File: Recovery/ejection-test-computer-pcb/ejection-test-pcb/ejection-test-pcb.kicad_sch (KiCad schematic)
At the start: 22 parts, among them J1 BATTERY_TERMINAL, J2 LOAD_CELL_CONNECTOR, J3 NICHROME-TERMINAL, Q1 IRLZ34N, SW1 ON, U1 HX7111, U2 LM2596, U3 ESP32_DEVKIT

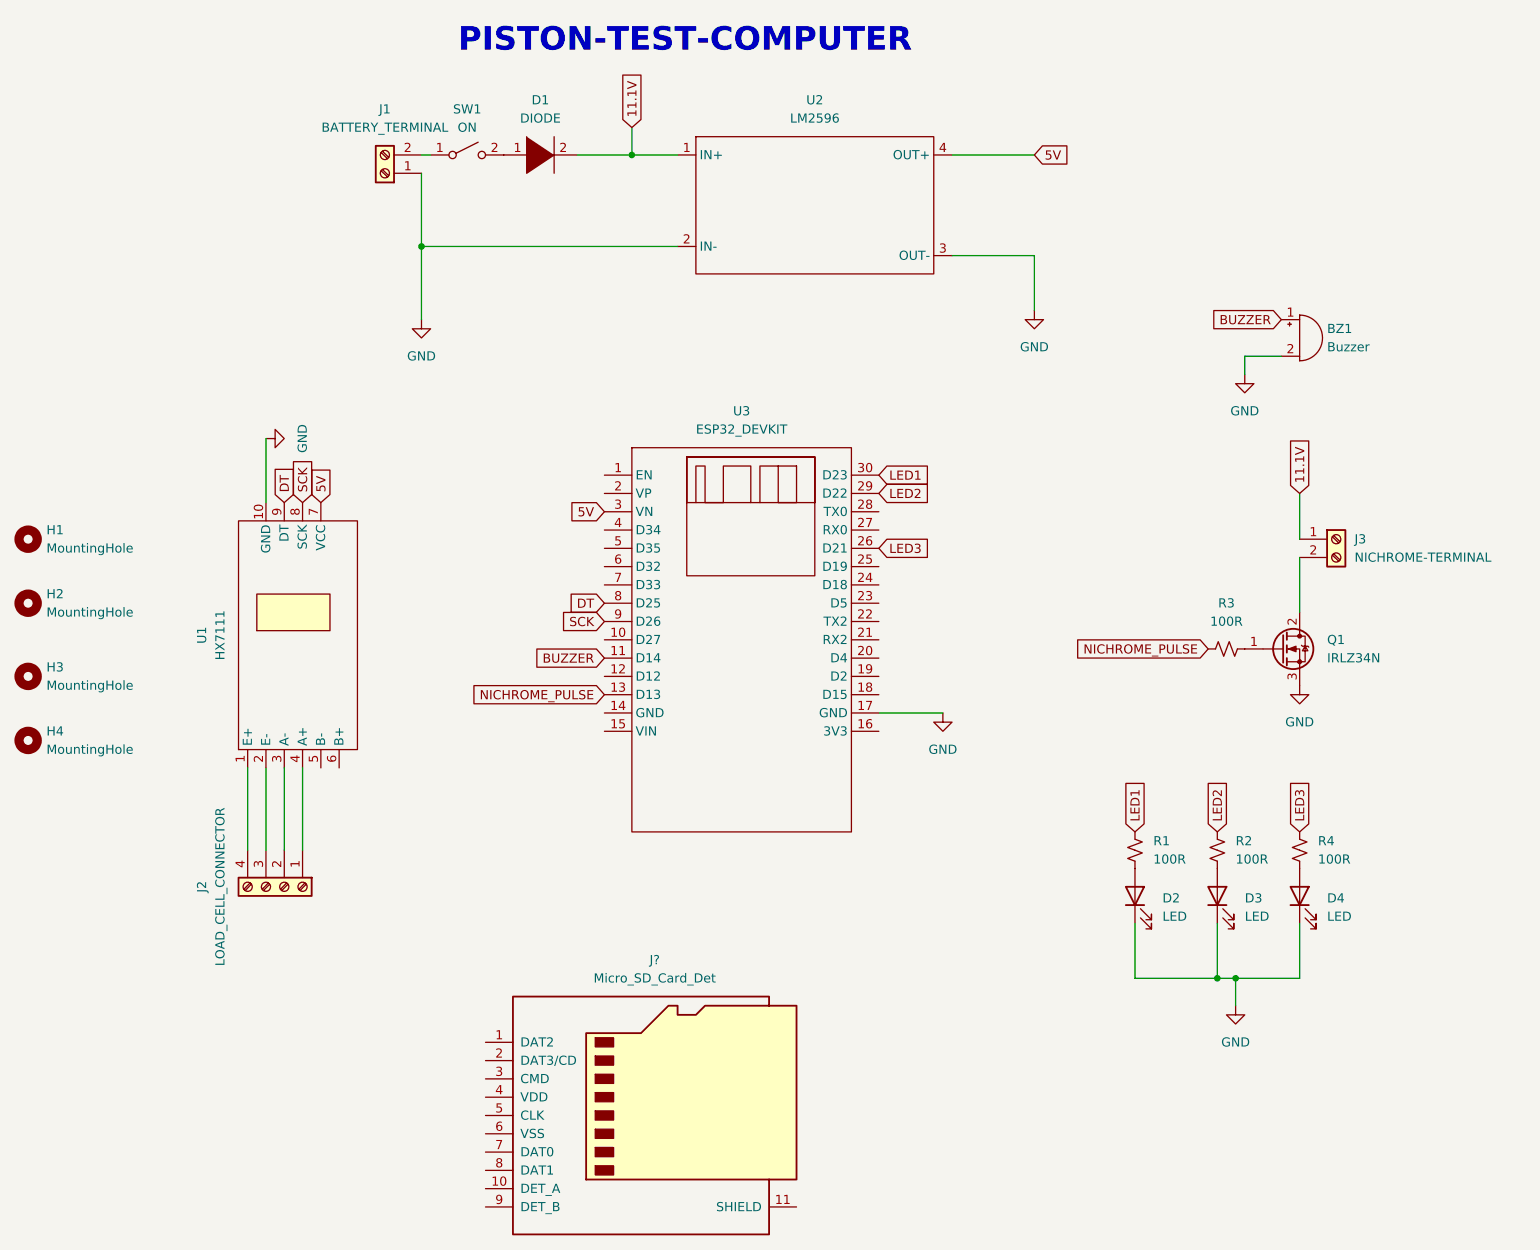
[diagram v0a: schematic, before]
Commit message: updated nichrome counter time
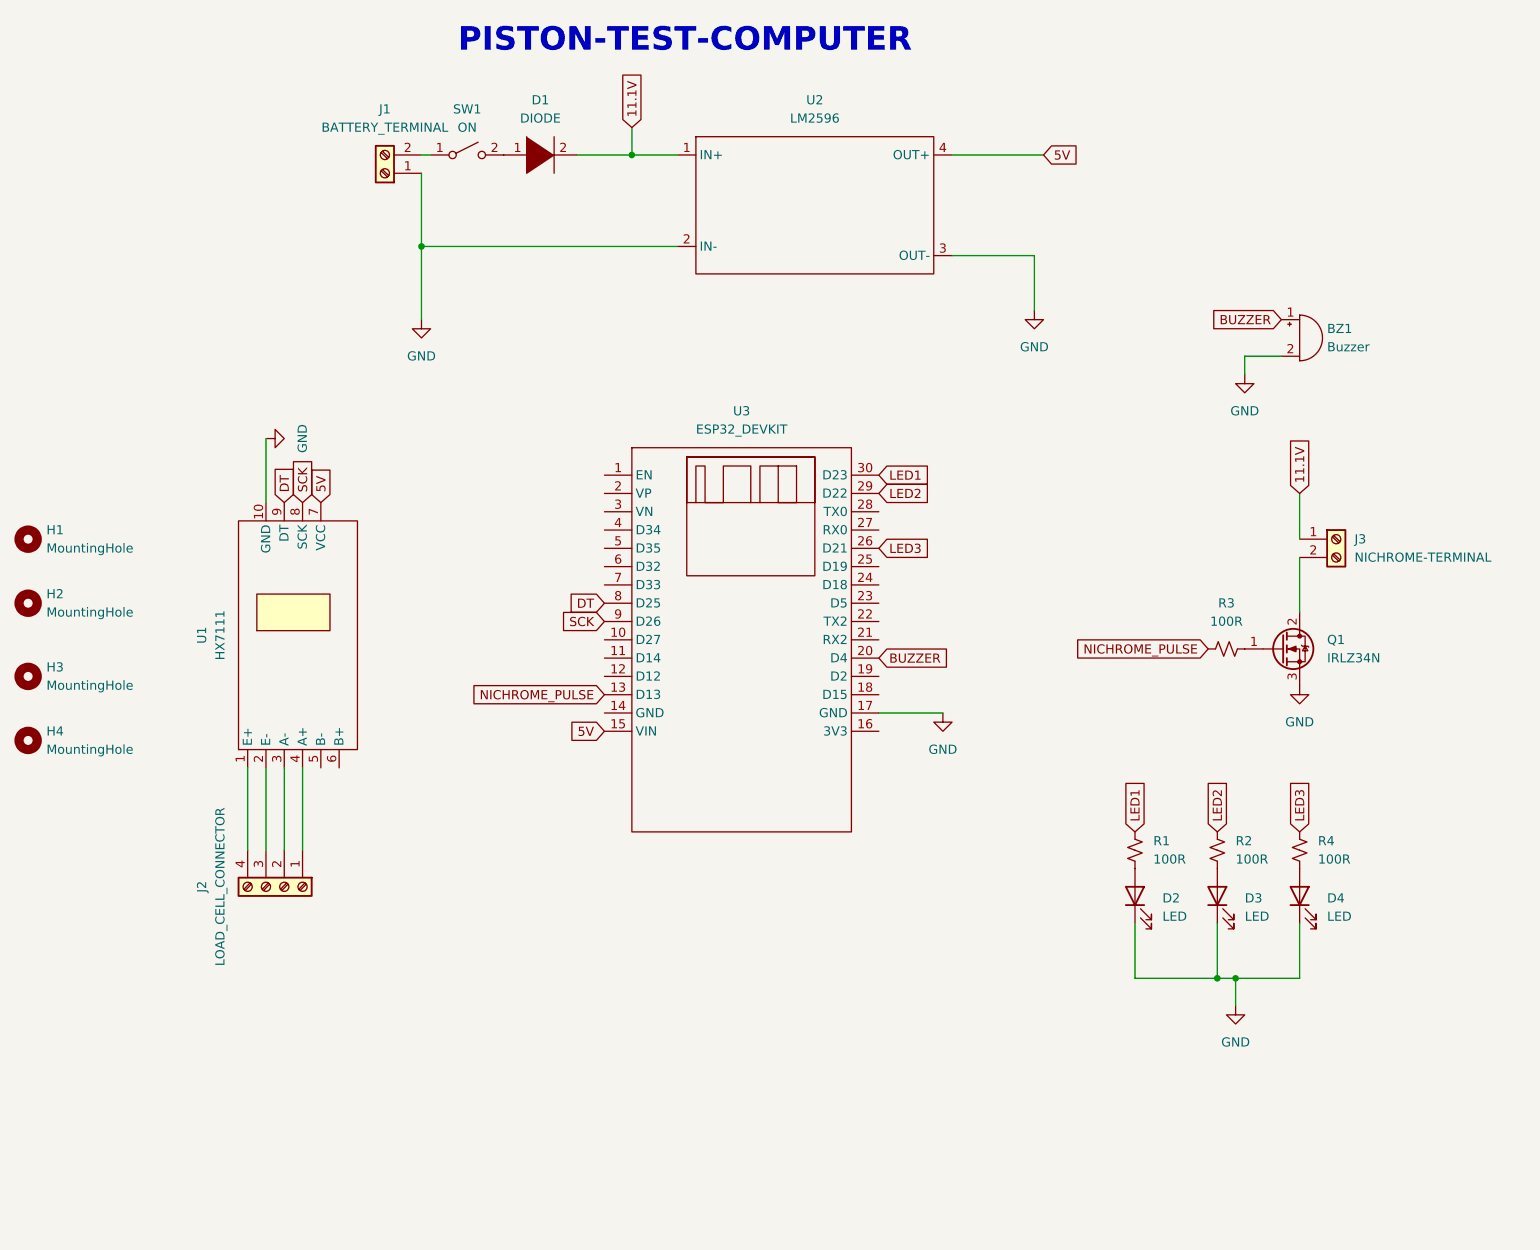
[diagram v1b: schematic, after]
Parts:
- removed J?: Micro_SD_Card_Det, symbol Connector:Micro_SD_Card_Det
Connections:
- net 5V: now also U3.15 (VIN); no longer U3.3 (VN)
- net BUZZER: now also U3.20 (D4); no longer U3.11 (D14)
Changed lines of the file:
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@@
     (stroke (width 0) (type default) (color 0 0 0 0))
   )
-  (wire (pts (xy 184.15 40.64) (xy 195.58 40.64))
+  (wire (pts (xy 184.15 40.64) (xy 196.85 40.64))
     (stroke (width 0) (type default) (color 0 0 0 0))
   )
@@
     )
   )
-  (global_label "5V" (shape input) (at 135.89 90.17 180) (fields_autoplaced)
+  (global_label "LED3" (shape input) (at 173.99 95.25 0) (fields_autoplaced)
+    (effects (font (size 1.27 1.27)) (justify left))
+    (property "Intersheet References" "${INTERSHEET_REFS}" (id 0) (at 181.0598 95.1706 0)
+      (effects (font (size 1.27 1.27)) (justify left) hide)
+    )
+  )
+  (global_label "5V" (shape input) (at 196.85 40.64 0) (fields_autoplaced)
+    (effects (font (size 1.27 1.27)) (justify left))
+    (property "Intersheet References" "${INTERSHEET_REFS}" (id 0) (at 201.5612 40.5606 0)
+      (effects (font (size 1.27 1.27)) (justify left) hide)
+    )
+  )
+  (global_label "LED1" (shape input) (at 209.55 134.62 90) (fields_autoplaced)
+    (effects (font (size 1.27 1.27)) (justify left))
+    (property "Intersheet References" "${INTERSHEET_REFS}" (id 0) (at 209.4706 127.5502 90)
+      (effects (font (size 1.27 1.27)) (justify left) hide)
+    )
+  )
+  (global_label "LED2" (shape input) (at 220.98 134.62 90) (fields_autoplaced)
+    (effects (font (size 1.27 1.27)) (justify left))
+    (property "Intersheet References" "${INTERSHEET_REFS}" (id 0) (at 220.9006 127.5502 90)
+      (effects (font (size 1.27 1.27)) (justify left) hide)
+    )
+  )
+  (global_label "11.1V" (shape input) (at 232.41 87.63 90) (fields_autoplaced)
+    (effects (font (size 1.27 1.27)) (justify left))
+    (property "Intersheet References" "${INTERSHEET_REFS}" (id 0) (at 232.3306 79.895 90)
+      (effects (font (size 1.27 1.27)) (justify left) hide)
+    )
+  )
+  (global_label "11.1V" (shape input) (at 139.7 36.83 90) (fields_autoplaced)
+    (effects (font (size 1.27 1.27)) (justify left))
+    (property "Intersheet References" "${INTERSHEET_REFS}" (id 0) (at 139.6206 29.095 90)
+      (effects (font (size 1.27 1.27)) (justify left) hide)
+    )
+  )
+  (global_label "5V" (shape input) (at 135.89 120.65 180) (fields_autoplaced)
     (effects (font (size 1.27 1.27)) (justify right))
-    (property "Intersheet References" "${INTERSHEET_REFS}" (id 0) (at 131.1788 90.0906 0)
+    (property "Intersheet References" "${INTERSHEET_REFS}" (id 0) (at 131.1788 120.7294 0)
       (effects (font (size 1.27 1.27)) (justify right) hide)
-    )
-  )
-  (global_label "LED3" (shape input) (at 173.99 95.25 0) (fields_autoplaced)
-    (effects (font (size 1.27 1.27)) (justify left))
-    (property "Intersheet References" "${INTERSHEET_REFS}" (id 0) (at 181.0598 95.1706 0)
-      (effects (font (size 1.27 1.27)) (justify left) hide)
-    )
-  )
-  (global_label "5V" (shape input) (at 195.58 40.64 0) (fields_autoplaced)
-    (effects (font (size 1.27 1.27)) (justify left))
-    (property "Intersheet References" "${INTERSHEET_REFS}" (id 0) (at 200.2912 40.5606 0)
-      (effects (font (size 1.27 1.27)) (justify left) hide)
-    )
-  )
-  (global_label "LED1" (shape input) (at 209.55 134.62 90) (fields_autoplaced)
-    (effects (font (size 1.27 1.27)) (justify left))
-    (property "Intersheet References" "${INTERSHEET_REFS}" (id 0) (at 209.4706 127.5502 90)
-      (effects (font (size 1.27 1.27)) (justify left) hide)
-    )
-  )
-  (global_label "LED2" (shape input) (at 220.98 134.62 90) (fields_autoplaced)
-    (effects (font (size 1.27 1.27)) (justify left))
-    (property "Intersheet References" "${INTERSHEET_REFS}" (id 0) (at 220.9006 127.5502 90)
-      (effects (font (size 1.27 1.27)) (justify left) hide)
-    )
-  )
-  (global_label "11.1V" (shape input) (at 232.41 87.63 90) (fields_autoplaced)
-    (effects (font (size 1.27 1.27)) (justify left))
-    (property "Intersheet References" "${INTERSHEET_REFS}" (id 0) (at 232.3306 79.895 90)
-      (effects (font (size 1.27 1.27)) (justify left) hide)
-    )
-  )
-  (global_label "11.1V" (shape input) (at 139.7 36.83 90) (fields_autoplaced)
-    (effects (font (size 1.27 1.27)) (justify left))
-    (property "Intersheet References" "${INTERSHEET_REFS}" (id 0) (at 139.6206 29.095 90)
-      (effects (font (size 1.27 1.27)) (justify left) hide)
     )
   )
@@
     )
   )
-  (global_label "BUZZER" (shape input) (at 135.89 110.49 180) (fields_autoplaced)
-    (effects (font (size 1.27 1.27)) (justify right))
-    (property "Intersheet References" "${INTERSHEET_REFS}" (id 0) (at 126.0383 110.4106 0)
-      (effects (font (size 1.27 1.27)) (justify right) hide)
+  (global_label "BUZZER" (shape input) (at 173.99 110.49 0) (fields_autoplaced)
+    (effects (font (size 1.27 1.27)) (justify left))
+    (property "Intersheet References" "${INTERSHEET_REFS}" (id 0) (at 183.8417 110.5694 0)
+      (effects (font (size 1.27 1.27)) (justify left) hide)
     )
   )
@@
     )
   )
-  (symbol (lib_id "Connector:Micro_SD_Card_Det") (at 142.24 173.99 0) (unit 1)
-    (in_bom yes) (on_board yes) (fields_autoplaced)
-    (property "Reference" "J?" (id 0) (at 142.875 152.4 0))
-    (property "Value" "Micro_SD_Card_Det" (id 1) (at 142.875 154.94 0))
-    (property "Footprint" "" (id 2) (at 194.31 156.21 0)
-      (effects (font (size 1.27 1.27)) hide)
-    )
-    (property "Datasheet" "https://www.hirose.com/product/en/download_file/key_name/DM3/category/Catalog/doc_file_id/49662/?file_category_id=4&item_id=195&is_series=1" (id 3) (at 142.24 171.45 0)
-      (effects (font (size 1.27 1.27)) hide)
-    )
-    (pin "1")
-    (pin "10")
-    (pin "11")
-    (pin "2")
-    (pin "3")
-    (pin "4")
-    (pin "5")
-    (pin "6")
-    (pin "7")
-    (pin "8")
-    (pin "9")
-  )
   (symbol (lib_id "power:GND") (at 195.58 62.23 0) (unit 1)
     (in_bom yes) (on_board yes) (fields_autoplaced)
@@
       (reference "J3") (unit 1) (value "NICHROME-TERMINAL") (footprint "TerminalBlock:TerminalBlock_bornier-2_P5.08mm")
     )
-    (path "/ab348d08-997e-4cc6-a582-90b9e2626bcc"
-      (reference "J?") (unit 1) (value "Micro_SD_Card_Det") (footprint "")
-    )
     (path "/5b7189bd-e7fc-4d66-b9af-d65b01750a9c"
